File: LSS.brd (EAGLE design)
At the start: 53.3 x 53.3 mm, 16 parts, among them J1 Digital_0_7, J2 Analog, J3 Digital_8_13

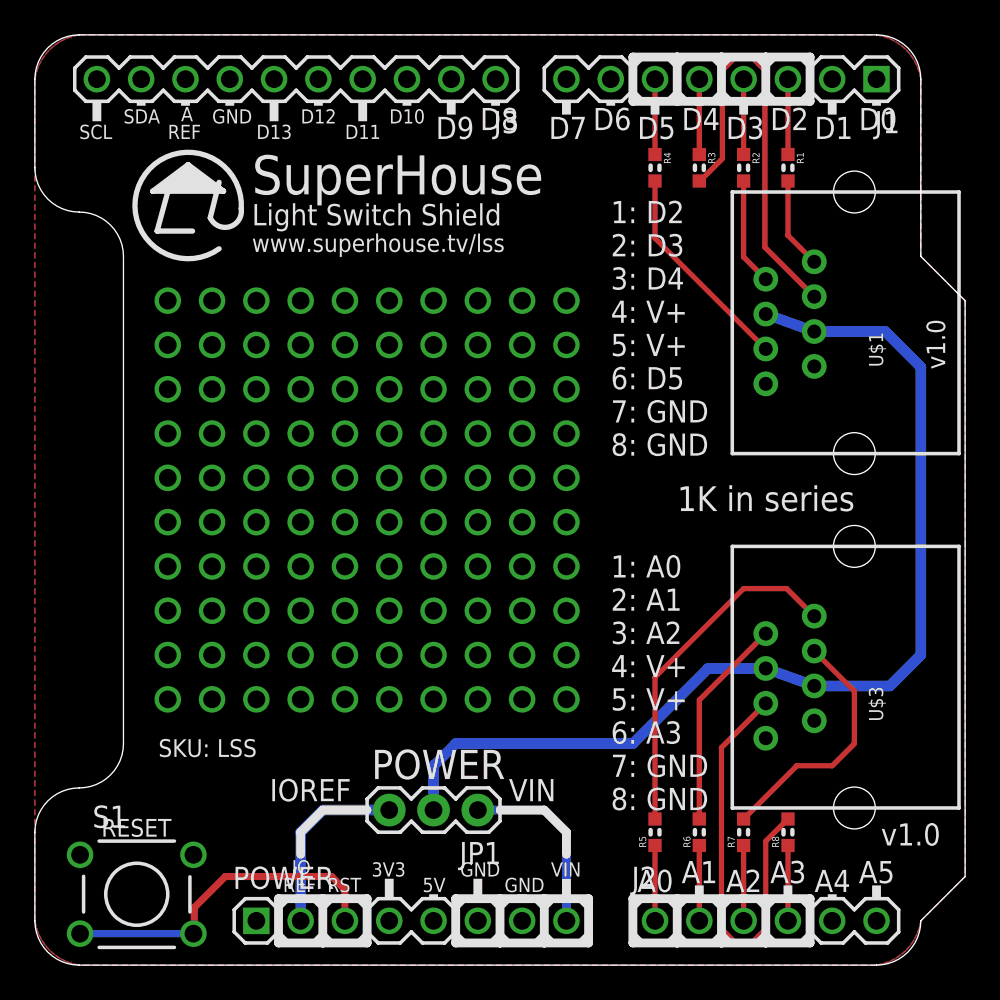
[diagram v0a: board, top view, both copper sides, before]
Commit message: Release v1.1 with D4 cleared to allow use on EtherTen
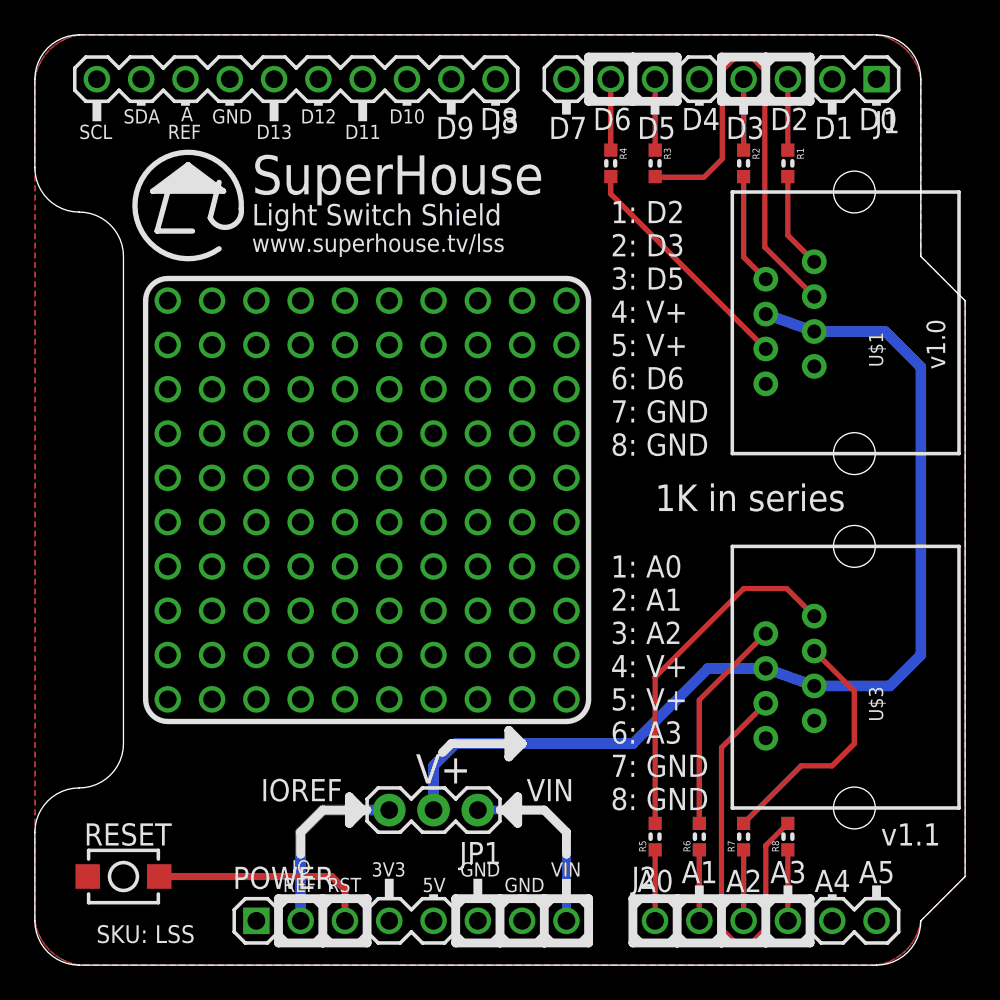
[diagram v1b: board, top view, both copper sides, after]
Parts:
- S1: device freetronics:TACTILE-PTH -> freetronics-jon:TACTILE_SWITCH_SMD_2PIN_TINY
- moved R3 2.55 mm to (35.6, 46.0)
- moved R4 2.55 mm to (33.0, 46.0)
- moved S1 1.27 mm to (5.08, 5.08), turned to 180 degrees
- moved R5 0.25 mm to (35.6, 7.37)
- moved R6 0.25 mm to (38.1, 7.37)
- moved R7 0.25 mm to (40.6, 7.37)
- moved R8 0.25 mm to (43.2, 7.37)
- moved R1 0.25 mm to (43.2, 46.0)
- moved R2 0.25 mm to (40.6, 46.0)
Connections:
- net D4: no longer R3.1
- net D5: now also R3.1; no longer R4.1
- net D6: now also R4.1
- net GND: no longer S1.1
- net RESET: now also S1.1; no longer S1.3, S1.4
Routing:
- net RESET: track 19.5 -> 12.7 mm
- net D4: track 4.32 -> 0.00 mm
- net D6: track 0.00 -> 4.06 mm
- net N$3: track 24.1 -> 26.6 mm
- net N$4: track 12.3 -> 13.6 mm
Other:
- board text added: "(C) 2019 SuperHouse Automation Pty Ltd Released under the TAPR Open Hardware License www.tapr.org/OHL"
- board text added: "1: D2 2: D3 3: D5 4: V+ 5: V+ 6: D6 7: GND 8: GND"
- board text added: "V+"
- board text added: "v1.1"
- board text removed: "(C) 2018 SuperHouse Automation Pty Ltd Released under the TAPR Open Hardware License www.tapr.org/OHL"
- board text removed: "1: D2 2: D3 3: D4 4: V+ 5: V+ 6: D5 7: GND 8: GND"
- board text removed: "POWER"
